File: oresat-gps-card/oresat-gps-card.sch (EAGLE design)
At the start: 367 parts, among them J1 ORESAT-DEBUG-CONNECTOR-CARD, J100 DM3BT-DSF-PEJS, J102 FTSH-105-XX-X-DV-K, J4 TFM-120-01-L-D-RA, Q1 MMBT2907, Q2 PMV45EN, Q3 DMP2240UDM, Q4 PMV45EN, Q5 MOSFET-PCH-SOT23-6, Q6 MOSFET-PCH-SOT23-6, U1 RCLAMP0504FB, U10 TLVH431, U11 TCAN330, U12 MIC842LYC5, U13 MIC842LYC5, U14 MAX4211FETE, U15 TPS62112, U16 MAX7310ATE, U17 25AAXX, U18 RCLAMP0504FB, U19 BP2G+, U2 TPS2051CDBVR, U20 MAX8510EXK29+T, U22 LT1719S6, U4 SN74LVC1G07DCK, U5 SKY65723-81, U6 7Q-16.368MBG-T, U7 OSD3358-512M-BSM, U8 MAX8510EXK29+T, U9 MAX8510EXK29+T, Y1 24MHz, Y2 ABS07-32.768KHZ-T

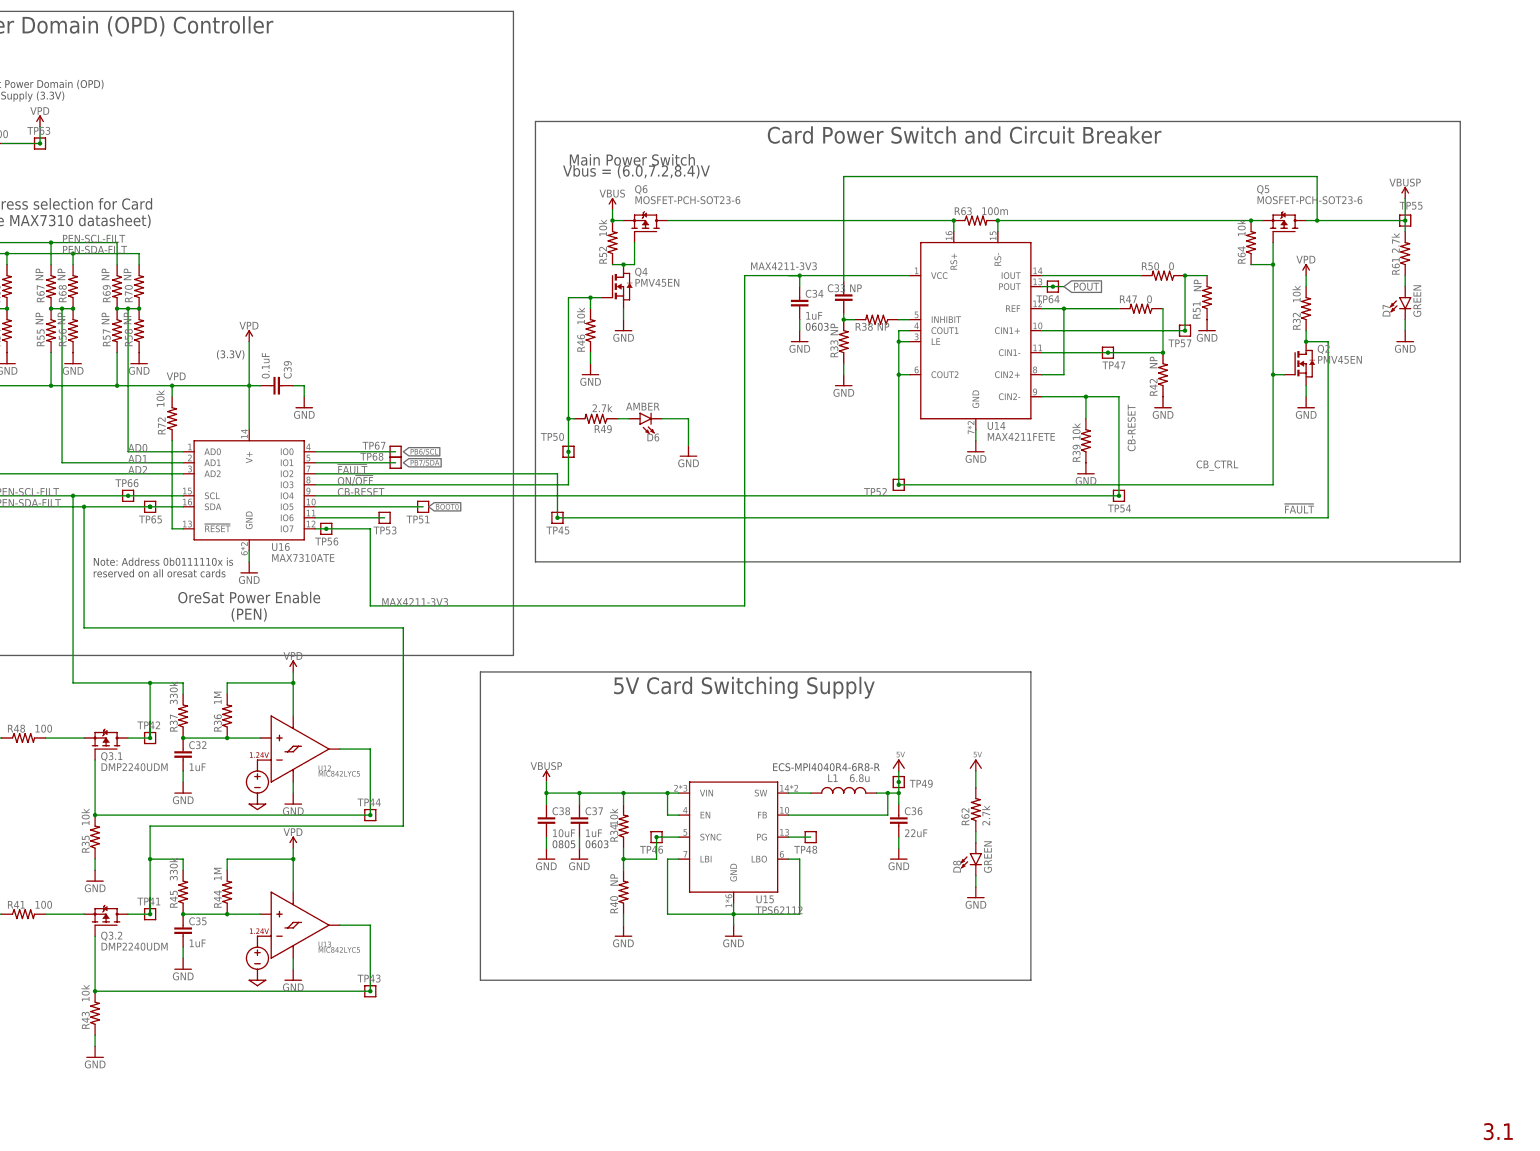
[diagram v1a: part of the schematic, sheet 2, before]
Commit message: Finished laying out Venus receiver. Fixed issue with GND and AGND planes. Added vias, and restrict lines to separate digital and RF ground planes. Added enable lines to Max and Venus receivers. Updated OPD circuit.
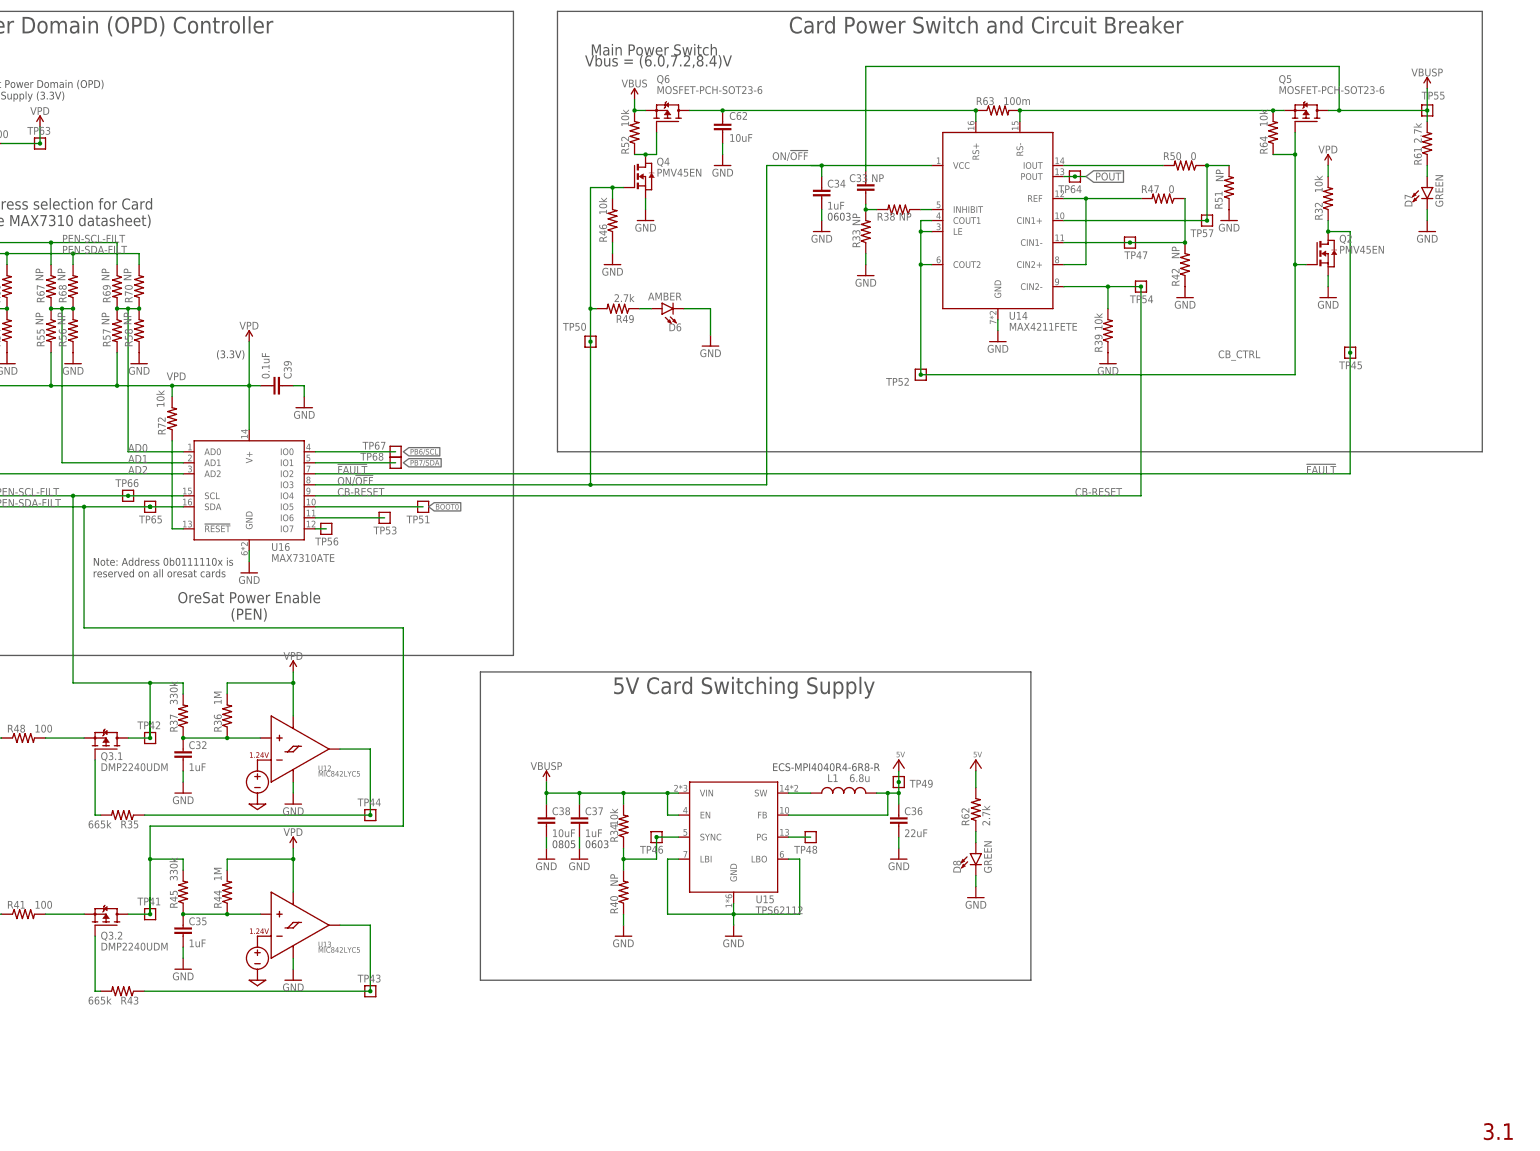
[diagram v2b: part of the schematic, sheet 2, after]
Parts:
- removed JP102, JP103, JP110, JP111: JUMPER-SMT_3_1-NC_TRACE_SILK, SparkFun-Jumpers:JUMPER-SMT_3_1-NC_TRACE_SILK
- added C62: 10uF, oresat-rcl:C-EU0805-B
- added R14, R18, R29, R30, R79, R80, R81: 10k, oresat-rcl:R-US_0603-B-NOSILK
- added TP71: TEST-POINT3X4, SparkFun-Connectors:TEST-POINT3X4
- R35, R43: value 10k -> 665k
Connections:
- removed net AGND: C16.2, C17.2, C20.2, C21.2, C25.2, C26.2, C27.2, C28.2, C44.2, C45.2, C51.2, C53.2, C56.2, C57.2, C58.2, C64.1, C81.2, CM1.SHIELD, CM1.SHIELD1, CM1.SHIELD2, CM1.SHIELD3, L8.GND@1, L8.GND@2, L8.GND@3, SH1.P$1, U$7.BODY, U$8.GND_RF, U19.GND, U5.GND, U6.GND1, U6.GND2
- removed net MAX4211-3V3: C34.1, TP56.1, U14.VCC, U16.IO7
- removed net N$132: JP102.2, U7C.MMC0_DAT3
- removed net N$133: TP19.1, U7D.MII1_RX_DV
- removed net N$50: JP103.2, U7C.MMC0_DAT2
- removed net SPI1_D1: TP18.1, U7D.MII1_RX_ER
- new net MAX-EN: R30.2, TP19.1, U7D.MII1_RX_DV, U8.EN, U9.EN
- new net N$122: R18.2, U$8.TXD0
- new net N$134: R29.2, U$8.PSE_SEL
- new net N$137: Q3.2.G, R43.2
- new net N$138: Q3.1.G, R35.2
- new net N$139: TP56.1, U16.IO7
- new net N$97: R14.2, U$8.RXD0
- new net STQ-EN: R79.2, TP18.1, U20.EN, U7D.MII1_RX_ER
- net 2.85V-S: now also R29.1, R80.1, R81.1
- net 3.3V: no longer U20.EN, U8.EN, U9.EN
- net GND: now also C16.2, C17.2, C20.2, C21.2, C25.2, C26.2, C27.2, C28.2, C44.2, C45.2, C51.2, C53.2, C56.2, C57.2, C58.2, C62.2, C64.1, C81.2, CM1.SHIELD, CM1.SHIELD1, CM1.SHIELD2, CM1.SHIELD3, L8.GND@1, L8.GND@2, L8.GND@3, R30.1, R79.1, SH1.P$1, U$7.BODY, U$8.GND_RF, U19.GND, U5.GND, U6.GND1, U6.GND2; no longer R35.1, R43.1
- net MAX-CLKOUT: now also TP71.1
- net N$21: now also R80.2, U$8.BAUDSEL0; no longer JP111.2, U7C.MMC0_DAT0
- net N$27: now also R35.1; no longer Q3.1.G, R35.2
- net N$32: now also R81.2, U$8.BAUDSEL1; no longer JP110.2, U7C.MMC0_DAT1
- net N$4: now also U7C.MMC0_DAT2; no longer JP103.3
- net N$5: now also U7C.MMC0_DAT3; no longer JP102.3
- net N$580: now also R43.1; no longer Q3.2.G, R43.2
- net N$8: now also U7C.MMC0_DAT0; no longer JP111.3
- net N$9: now also U7C.MMC0_DAT1; no longer JP110.3
- net N$98: now also C62.1
- net ON/!OFF: now also C34.1, U14.VCC
- net UART2_RX: now also R18.1; no longer U$8.TXD0
- net UART2_TX: now also R14.1; no longer U$8.RXD0
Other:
- note added: "1.2V LDO out Noconnect"
- note added: "2.85V analog supply for MAX2771"
- note added: "2.85V digital supply for MAX2771"
- note added: "MAX2771 SPI CONFIG port"
- note added: "Outputs on GPIO2,3 and inputs on GPIO0."
- note added: "To Skytraq Receiver: UART2_RX == MII1_TX_CLK UART2_TX == MII1_RX_CLK"
- note removed: "1.2V LDO out"
- note removed: "2.85V analog supply for MAX2769"
- note removed: "2.85V digital supply for MAX2769"
- note removed: "MAX2769 SPI CONFIG port"
- note removed: "NOTE: All these signals are outputs with the exception of FLASH. Likewise, I put the outputs on GPIO2,3 and inputs on GPIO0. I am not sure if this is better, but it seemed logical"
- note removed: "To Skytraq Receiver: UART2 RX == MII1_TX_CLK UART2 TX == MII1_RX_CLK"
- moved on the sheet: C33, C34, D6, D7, Q2, Q4, Q5, Q6, R32, R33, R35, R38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
